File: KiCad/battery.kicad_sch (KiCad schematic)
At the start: 8 parts, among them U12 BQ25185DLHR

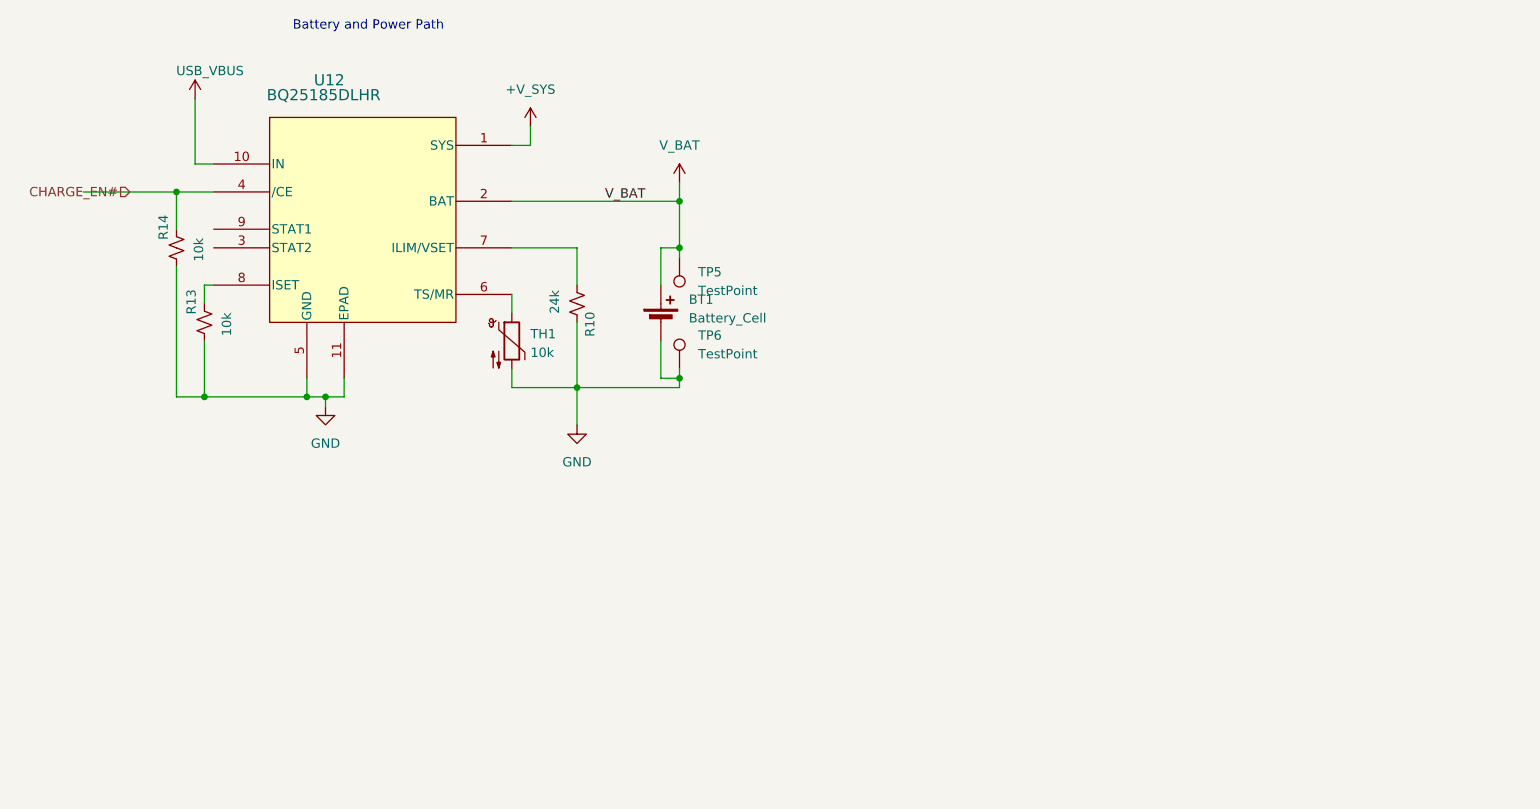
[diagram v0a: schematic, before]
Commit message: Start of docs and design incremental progress
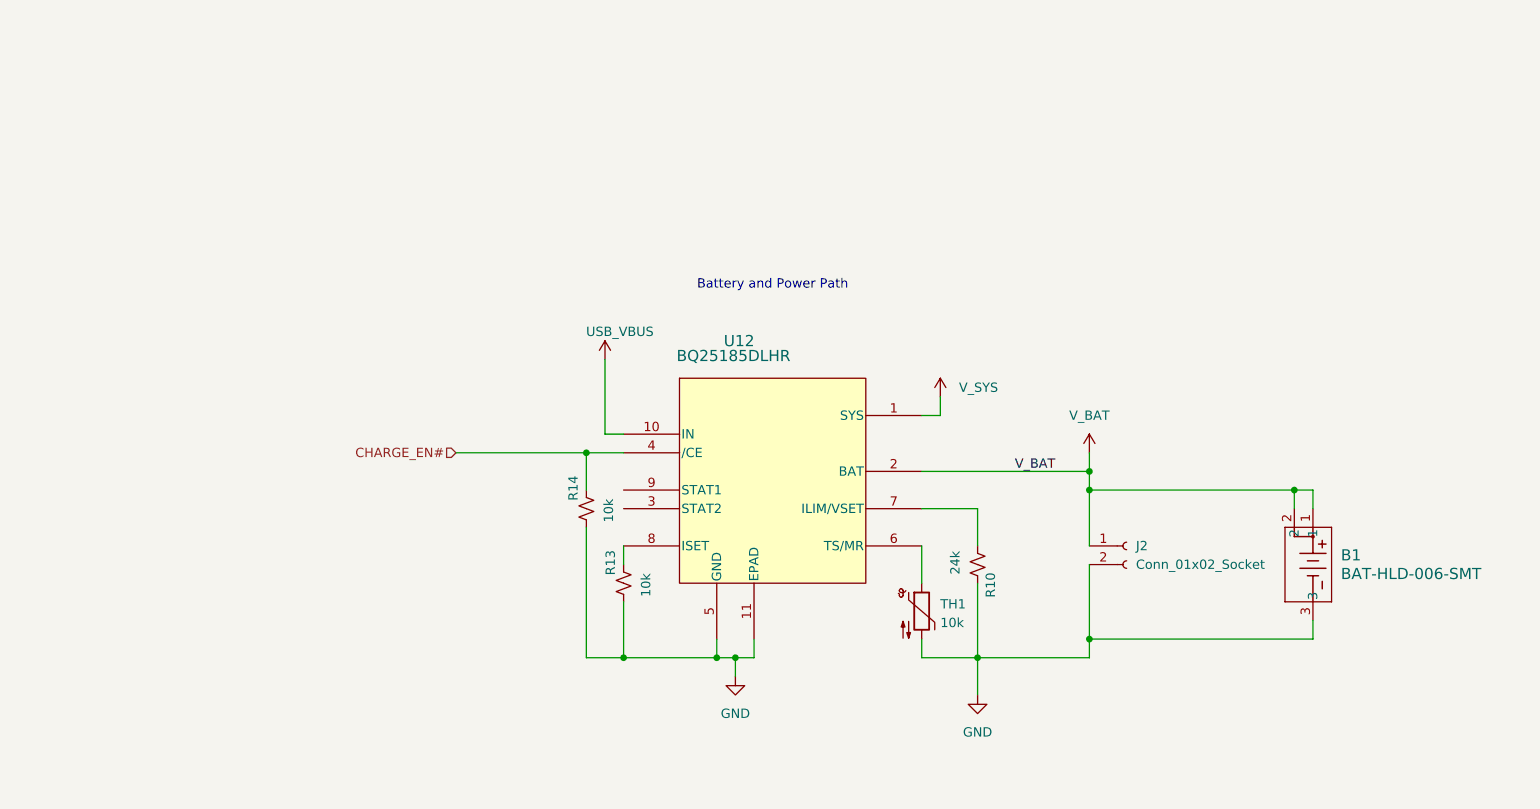
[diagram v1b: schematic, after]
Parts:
- removed BT1: Battery_Cell, symbol Device:Battery_Cell
- removed TP5, TP6: TestPoint, symbol Connector:TestPoint
- added B1: BAT-HLD-006-SMT, JetBoard:BAT-HLD-006-SMT_LNX, symbol 2025-03-15_22-46-16:BAT-HLD-006-SMT
- added J2: Conn_01x02_Socket, Connector_JST:JST_GH_BM02B-GHS-TBT_1x02-1MP_P1.25mm_Vertical, symbol Connector:Conn_01x02_Socket
- TH1: footprint (none) -> Resistor_SMD:R_0402_1005Metric
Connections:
- net GND: now also B1.3, J2.2 (Pin_2)
- net V_BAT: now also B1.1, B1.2, J2.1 (Pin_1)
- net +V_SYS renamed V_SYS
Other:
- moved on the sheet: R10, R13, R14, TH1, U12

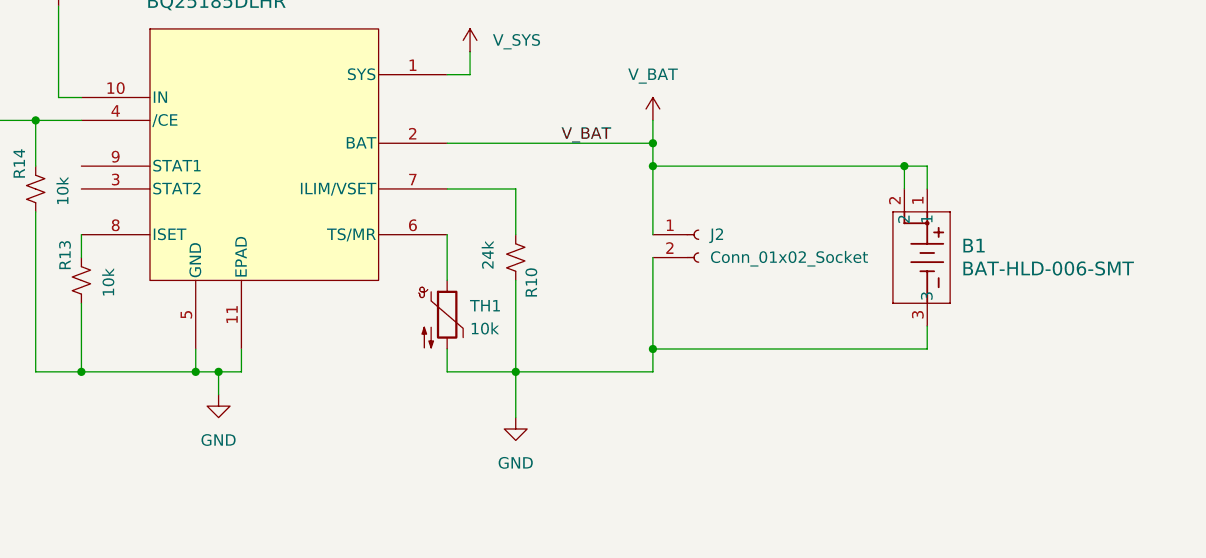
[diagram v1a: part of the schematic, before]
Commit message: Schematic changes
- Changed to STM8L050
- Changed to SPI interface for STM8 bootloader
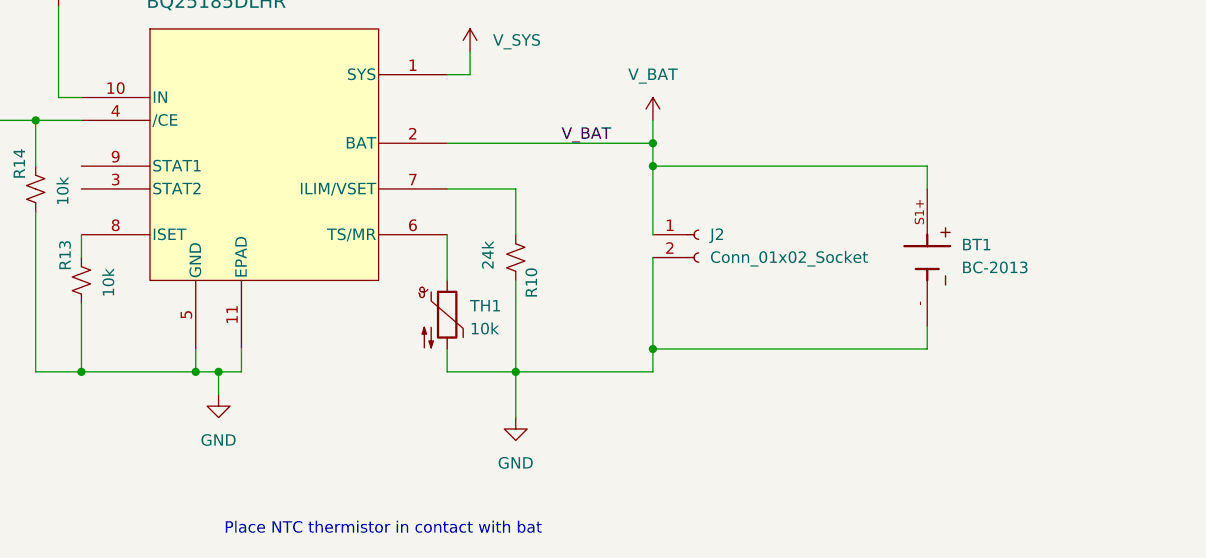
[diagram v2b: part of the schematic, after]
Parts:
- removed B1: BAT-HLD-006-SMT, JetBoard:BAT-HLD-006-SMT_LNX, symbol 2025-03-15_22-46-16:BAT-HLD-006-SMT
- added BT1: BC-2013, JetBoard:BAT_BC-2013, symbol Connector:BC-2013
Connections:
- net GND: now also BT1.-
- net V_BAT: now also BT1.S1+
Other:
- note added: "Place NTC thermistor in contact with bat"
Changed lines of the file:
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@@
 	(generator_version "9.0")
 	(paper "A4")
+	(text "Place NTC thermistor in contact with bat"
+		(exclude_from_sim no)
+		(at 150.368 139.446 0)
+		(effects
+			(font
+				(size 1.27 1.27)
+			)
+		)
+	)
 	(text "Battery and Power Path"
 		(exclude_from_sim no)
@@
 	)
 	(junction
-		(at 208.28 99.06)
-		(diameter 0)
-		(color 0 0 0 0)
-	)
-	(junction
 		(at 165.1 121.92)
 		(diameter 0)
@@
 	(wire
 		(pts
-			(xy 180.34 99.06) (xy 208.28 99.06)
+			(xy 180.34 99.06) (xy 210.82 99.06)
 		)
 		(stroke
@@
 	(wire
 		(pts
-			(xy 208.28 101.6) (xy 208.28 99.06)
-		)
-		(stroke
-			(width 0)
-			(type default)
-		)
-	)
-	(wire
-		(pts
 			(xy 165.1 101.6) (xy 165.1 106.68)
 		)
@@
 		(pts
 			(xy 157.48 96.52) (xy 180.34 96.52)
-		)
-		(stroke
-			(width 0)
-			(type default)
-		)
-	)
-	(wire
-		(pts
-			(xy 208.28 99.06) (xy 210.82 99.06)
 		)
 		(stroke
@@
 	)
 	(symbol
-		(lib_id "2025-03-15_22-46-16:BAT-HLD-006-SMT")
-		(at 210.82 101.6 270)
-		(unit 1)
-		(exclude_from_sim no)
-		(in_bom yes)
-		(on_board yes)
-		(dnp no)
-		(fields_autoplaced yes)
-		(property "Reference" "B1"
-			(at 214.63 107.9499 90)
-			(effects
-				(font
-					(size 1.524 1.524)
-				)
-				(justify left)
-			)
-		)
-		(property "Value" "BAT-HLD-006-SMT"
-			(at 214.63 110.4899 90)
-			(effects
-				(font
-					(size 1.524 1.524)
-				)
-				(justify left)
-			)
-		)
-		(property "Footprint" "JetBoard:BAT-HLD-006-SMT_LNX"
-			(at 210.82 101.6 0)
-			(effects
-				(font
-					(size 1.27 1.27)
-					(italic yes)
-				)
-				(hide yes)
-			)
-		)
-		(property "Datasheet" "BAT-HLD-006-SMT"
-			(at 210.82 101.6 0)
-			(effects
-				(font
-					(size 1.27 1.27)
-					(italic yes)
-				)
-				(hide yes)
-			)
-		)
-		(property "Description" ""
-			(at 210.82 101.6 0)
-			(effects
-				(font
-					(size 1.27 1.27)
-				)
-				(hide yes)
-			)
-		)
-		(pin "1"
-		)
-		(pin "2"
-		)
-		(pin "3"
-		)
-		(instances
-			(project ""
-				(path "/6338cb95-8536-41ae-a90a-0bf3cec19d9d/ac09af11-5794-40a5-ab3d-ac2e3f5d0ff8"
-					(reference "B1")
-					(unit 1)
-				)
-			)
-		)
-	)
-	(symbol
 		(lib_id "Connector:Conn_01x02_Socket")
 		(at 185.42 106.68 0)
@@
 					(unit 1)
 				)
+			)
+		)
+	)
+	(symbol
+		(lib_id "Connector:BC-2013")
+		(at 210.82 109.22 270)
+		(unit 1)
+		(exclude_from_sim no)
+		(in_bom yes)
+		(on_board yes)
+		(dnp no)
+		(fields_autoplaced yes)
+		(property "Reference" "BT1"
+			(at 214.63 107.8229 90)
+			(effects
+				(font
+					(size 1.27 1.27)
+				)
+				(justify left)
+			)
+		)
+		(property "Value" "BC-2013"
+			(at 214.63 110.3629 90)
+			(effects
+				(font
+					(size 1.27 1.27)
+				)
+				(justify left)
+			)
+		)
+		(property "Footprint" "JetBoard:BAT_BC-2013"
+			(at 210.82 109.22 0)
+			(effects
+				(font
+					(size 1.27 1.27)
+				)
+				(justify bottom)
+				(hide yes)
+			)
+		)
+		(property "Datasheet" ""
+			(at 210.82 109.22 0)
+			(effects
+				(font
+					(size 1.27 1.27)
+				)
+				(hide yes)
+			)
+		)
+		(property "Description" ""
+			(at 210.82 109.22 0)
+			(effects
+				(font
+					(size 1.27 1.27)
+				)
+				(hide yes)
+			)
+		)
+		(property "PARTREV" "D"
+			(at 210.82 109.22 0)
+			(effects
+				(font
+					(size 1.27 1.27)
+				)
+				(justify bottom)
+				(hide yes)
+			)
+		)
+		(property "STANDARD" "Manufacturer Recommendations"
+			(at 210.82 109.22 0)
+			(effects
+				(font
+					(size 1.27 1.27)
+				)
+				(justify bottom)
+				(hide yes)
+			)
+		)
+		(property "MAXIMUM_PACKAGE_HEIGHT" "3.68mm"
+			(at 210.82 109.22 0)
+			(effects
+				(font
+					(size 1.27 1.27)
+				)
+				(justify bottom)
+				(hide yes)
+			)
+		)
+		(property "MANUFACTURER" "MPD"
+			(at 210.82 109.22 0)
+			(effects
+				(font
+					(size 1.27 1.27)
+				)
+				(justify bottom)
+				(hide yes)
+			)
+		)
+		(pin "-"
+		)
+		(pin "S1+"
+		)
+		(instances
+			(project ""
+				(path "/6338cb95-8536-41ae-a90a-0bf3cec19d9d/ac09af11-5794-40a5-ab3d-ac2e3f5d0ff8"
+					(reference "BT1")
+					(unit 1)
+				)

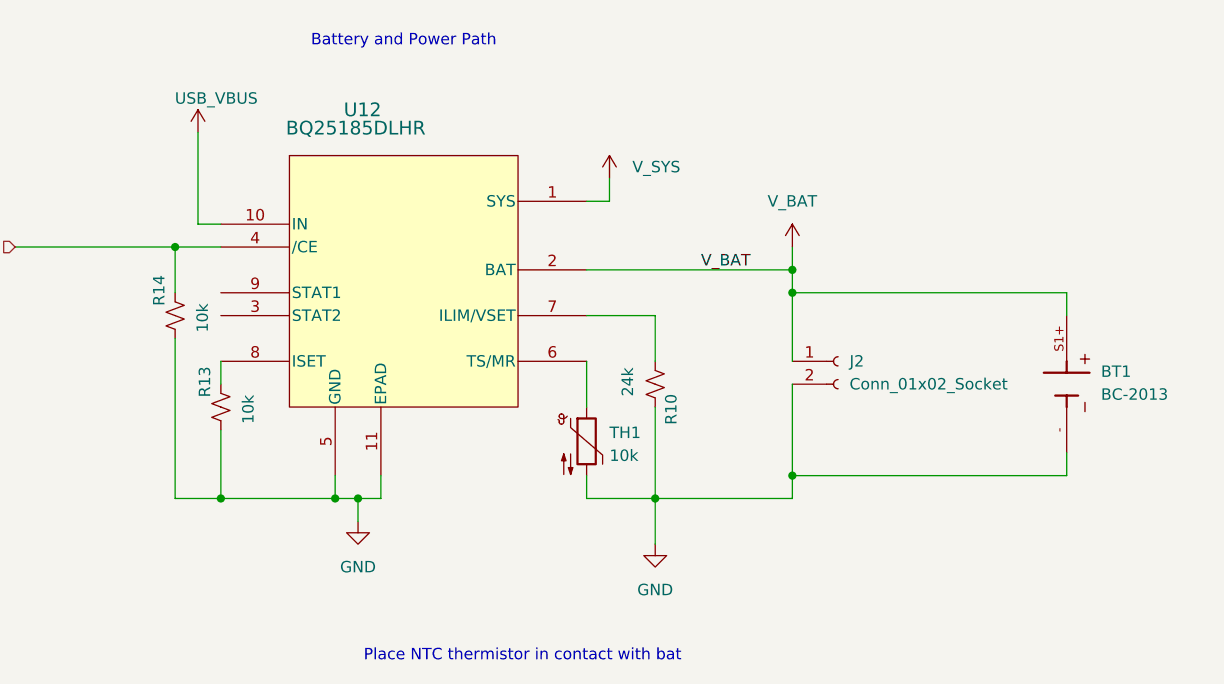
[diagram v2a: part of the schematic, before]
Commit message: Clean up ERC errors
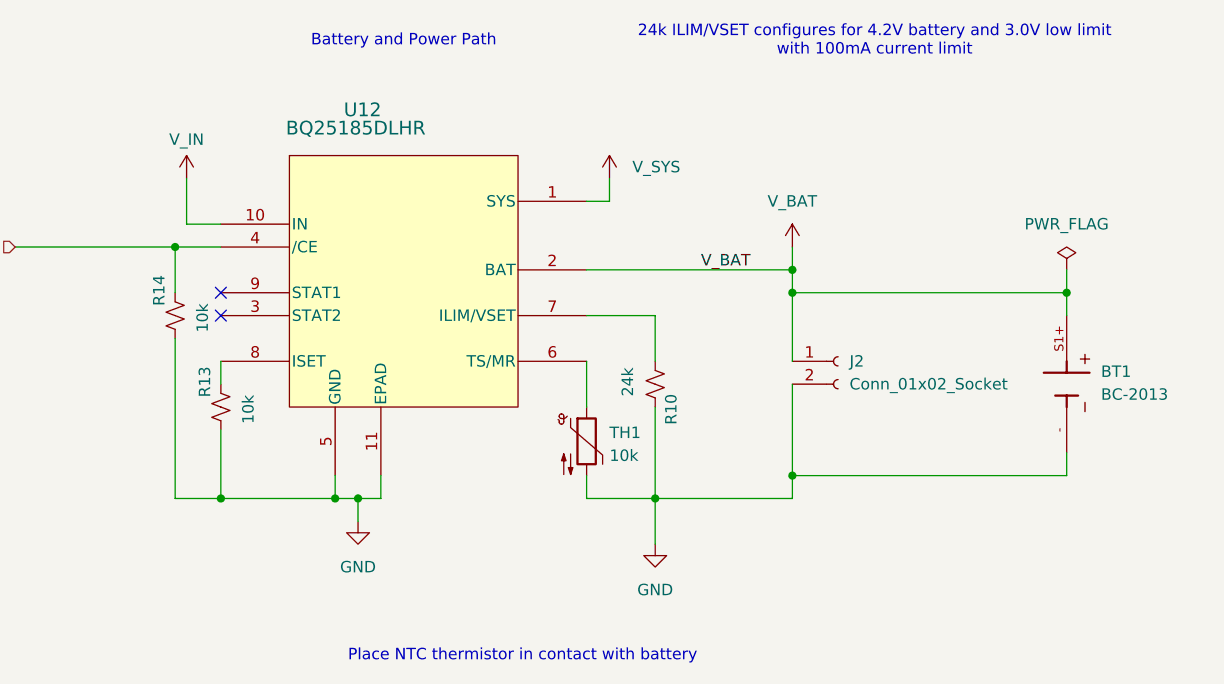
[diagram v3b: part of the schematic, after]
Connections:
- net USB_VBUS renamed V_IN
- no-connect marks 0 -> 2
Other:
- note added: "24k ILIM/VSET configures for 4.2V battery and 3.0V low limit with 100mA current limit"
- note added: "Place NTC thermistor in contact with battery"
- note removed: "Place NTC thermistor in contact with bat"
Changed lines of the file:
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@@
 	(generator_version "9.0")
 	(paper "A4")
-	(text "Place NTC thermistor in contact with bat"
+	(text "24k ILIM/VSET configures for 4.2V battery and 3.0V low limit\nwith 100mA current limit"
+		(exclude_from_sim no)
+		(at 189.484 71.12 0)
+		(effects
+			(font
+				(size 1.27 1.27)
+			)
+		)
+	)
+	(text "Place NTC thermistor in contact with battery"
 		(exclude_from_sim no)
 		(at 150.368 139.446 0)
@@
 	)
 	(junction
+		(at 210.82 99.06)
+		(diameter 0)
+		(color 0 0 0 0)
+	)
+	(junction
 		(at 165.1 121.92)
 		(diameter 0)
@@
 		(color 0 0 0 0)
 	)
+	(no_connect
+		(at 116.84 101.6)
+	)
+	(no_connect
+		(at 116.84 99.06)
+	)
 	(wire
 		(pts
@@
 	(wire
 		(pts
+			(xy 210.82 96.52) (xy 210.82 99.06)
+		)
+		(stroke
+			(width 0)
+			(type default)
+		)
+	)
+	(wire
+		(pts
 			(xy 180.34 119.38) (xy 180.34 121.92)
 		)
@@
 	(wire
 		(pts
-			(xy 114.3 81.28) (xy 114.3 91.44)
+			(xy 113.03 86.36) (xy 113.03 91.44)
 		)
 		(stroke
@@
 	(wire
 		(pts
-			(xy 116.84 91.44) (xy 114.3 91.44)
+			(xy 116.84 91.44) (xy 113.03 91.44)
 		)
 		(stroke
@@
 		)
 	)
+	(netclass_flag ""
+		(length 2.54)
+		(shape round)
+		(at 165.1 96.52 0)
+		(fields_autoplaced yes)
+		(effects
+			(font
+				(size 1.27 1.27)
+			)
+			(justify left bottom)
+		)
+		(property "Netclass" "Power"
+			(at 165.7985 93.98 0)
+			(effects
+				(font
+					(size 1.27 1.27)
+				)
+				(justify left)
+			)
+		)
+		(property "Component Class" ""
+			(at -49.53 19.05 0)
+			(effects
+				(font
+					(size 1.27 1.27)
+					(italic yes)
+				)
+			)
+		)
+	)
 	(symbol
 		(lib_id "Device:R_Small_US")
@@
 	(symbol
 		(lib_id "power:+3.3V")
-		(at 114.3 81.28 0)
+		(at 113.03 86.36 0)
 		(unit 1)
 		(exclude_from_sim no)
@@
 		(dnp no)
 		(property "Reference" "#PWR036"
-			(at 114.3 85.09 0)
-			(effects
-				(font
-					(size 1.27 1.27)
-				)
-				(hide yes)
-			)
-		)
-		(property "Value" "USB_VBUS"
-			(at 116.332 77.47 0)
+			(at 113.03 90.17 0)
+			(effects
+				(font
+					(size 1.27 1.27)
+				)
+				(hide yes)
+			)
+		)
+		(property "Value" "V_IN"
+			(at 113.03 82.042 0)
 			(effects
 				(font
@@
 		)
 		(property "Footprint" ""
-			(at 114.3 81.28 0)
+			(at 113.03 86.36 0)
 			(effects
 				(font
@@
 		)
 		(property "Datasheet" ""
-			(at 114.3 81.28 0)
+			(at 113.03 86.36 0)
 			(effects
 				(font
@@
 		)
 		(property "Description" "Power symbol creates a global label with name \"+3.3V\""
-			(at 114.3 81.28 0)
+			(at 113.03 86.36 0)
 			(effects
 				(font
@@
 					(unit 1)
 				)
+			)
+		)
+	)
+	(symbol
+		(lib_id "power:PWR_FLAG")
+		(at 210.82 96.52 0)
+		(unit 1)
+		(exclude_from_sim no)
+		(in_bom yes)
+		(on_board yes)
+		(dnp no)
+		(fields_autoplaced yes)
+		(property "Reference" "#FLG04"
+			(at 210.82 94.615 0)
+			(effects
+				(font
+					(size 1.27 1.27)
+				)
+				(hide yes)
+			)
+		)
+		(property "Value" "PWR_FLAG"
+			(at 210.82 91.44 0)
+			(effects
+				(font
+					(size 1.27 1.27)
+				)
+			)
+		)
+		(property "Footprint" ""
+			(at 210.82 96.52 0)
+			(effects
+				(font
+					(size 1.27 1.27)
+				)
+				(hide yes)
+			)
+		)
+		(property "Datasheet" "~"
+			(at 210.82 96.52 0)
+			(effects
+				(font
+					(size 1.27 1.27)
+				)
+				(hide yes)
+			)
+		)
+		(property "Description" "Special symbol for telling ERC where power comes from"
+			(at 210.82 96.52 0)
+			(effects
+				(font
+					(size 1.27 1.27)
+				)
+				(hide yes)
+			)
+		)
+		(pin "1"
+		)
+		(instances
+			(project ""
+				(path "/6338cb95-8536-41ae-a90a-0bf3cec19d9d/ac09af11-5794-40a5-ab3d-ac2e3f5d0ff8"
+					(reference "#FLG04")
+					(unit 1)
+				)
